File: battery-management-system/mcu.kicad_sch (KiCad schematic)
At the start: 28 parts, among them J11 I2C, J12 MCU_SUPPLY, J13 LEDS, U4 STM32L071CZTx, U5 ARM-JTAG-SWD, U8 AT24C512C, U9 NCT75DR2G

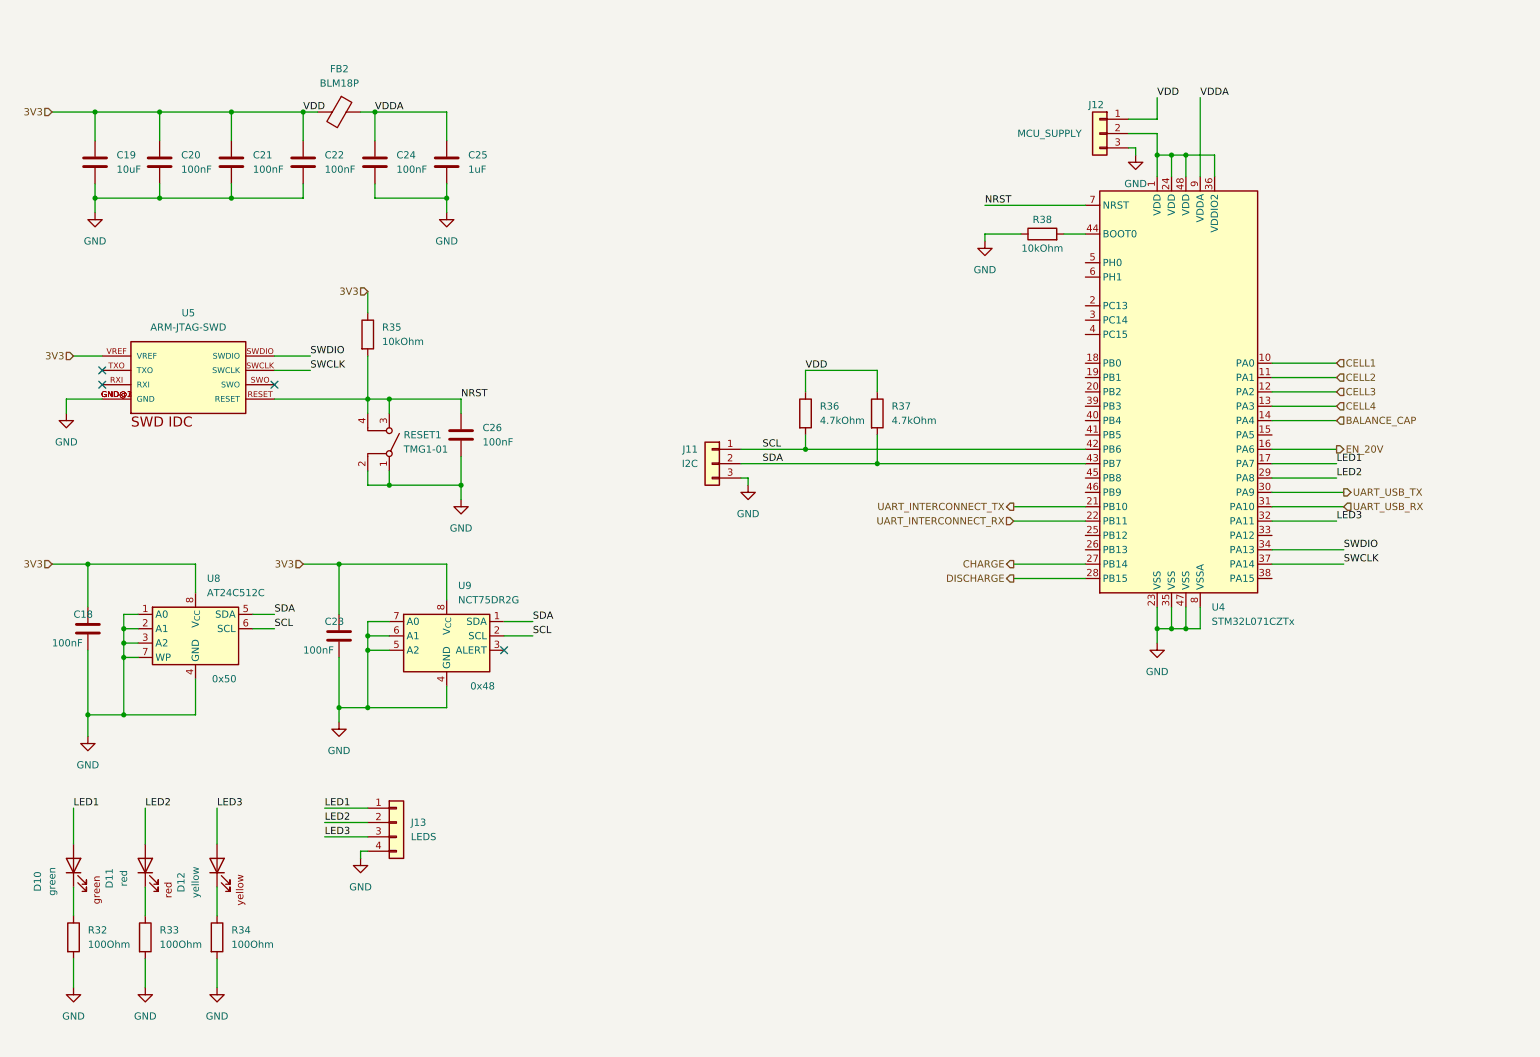
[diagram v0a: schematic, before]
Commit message: improve usage of net labels
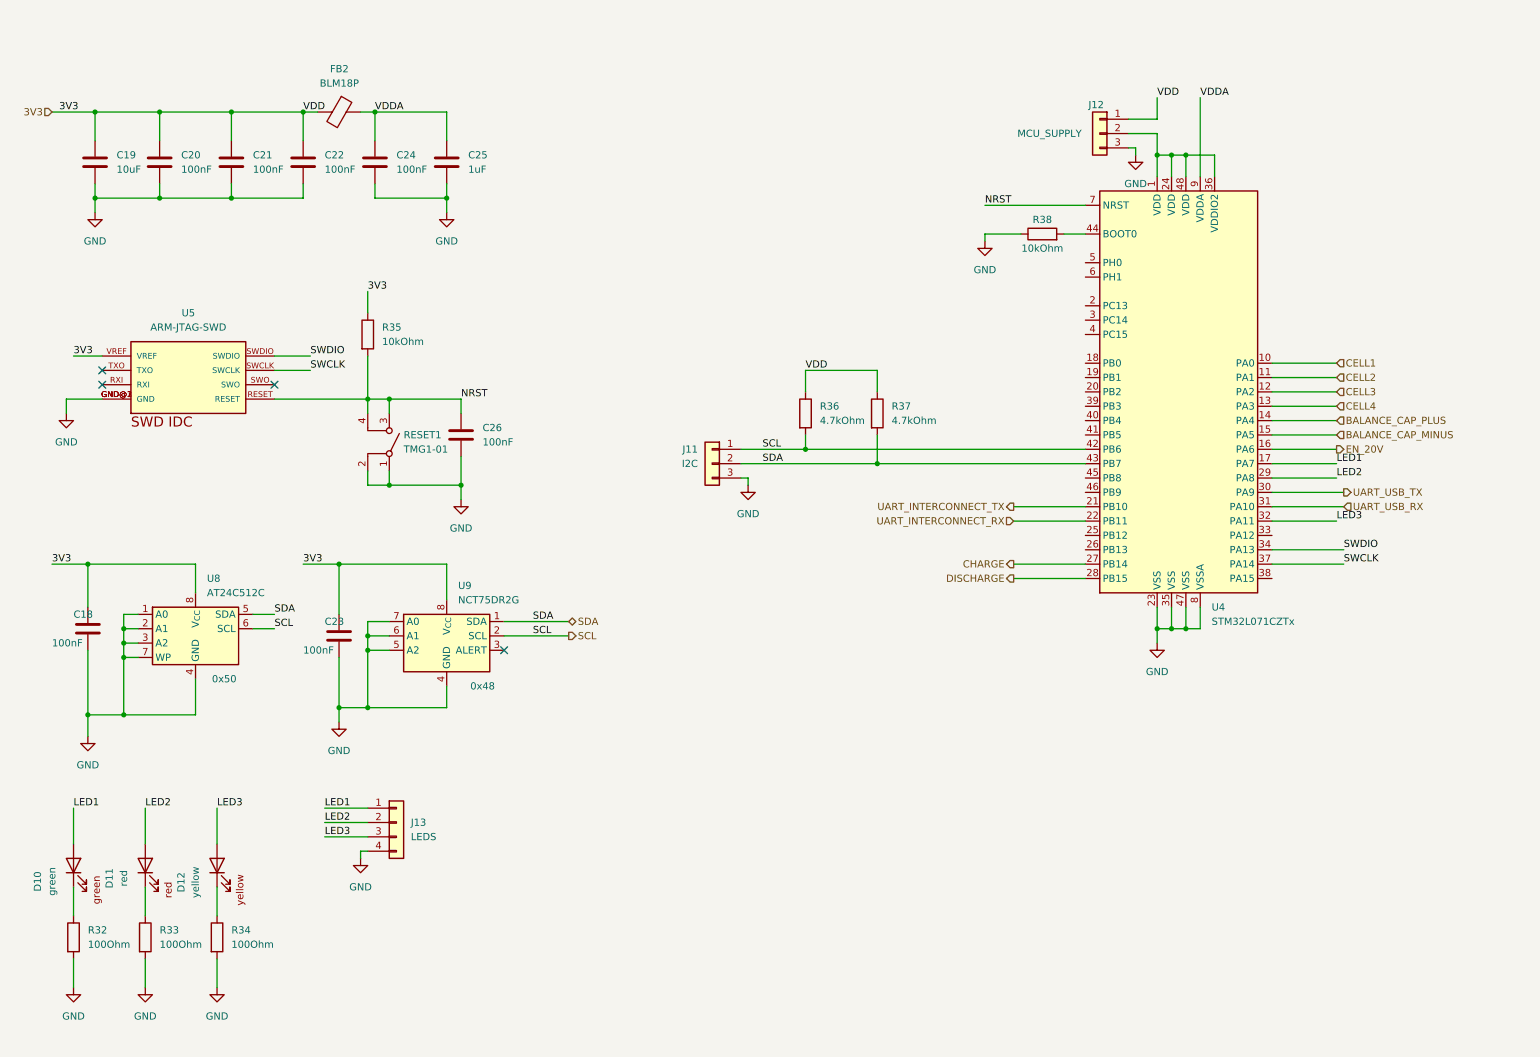
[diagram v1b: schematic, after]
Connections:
- net BALANCE_CAP_MINUS: now reaches U4.15 (PA5)
- net BALANCE_CAP renamed BALANCE_CAP_PLUS
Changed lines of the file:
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@@
     (stroke (width 0) (type default))
   )
-  (wire (pts (xy 104.14 120.65) (xy 109.22 120.65))
+  (wire (pts (xy 104.14 120.65) (xy 115.57 120.65))
     (stroke (width 0) (type default))
   )
@@
     (stroke (width 0) (type default))
   )
+  (wire (pts (xy 240.03 87.63) (xy 251.46 87.63))
+    (stroke (width 0) (type default))
+  )
   (wire (pts (xy 222.25 38.1) (xy 222.25 41.91))
     (stroke (width 0) (type default))
@@
     (stroke (width 0) (type default))
   )
-  (wire (pts (xy 104.14 123.19) (xy 109.22 123.19))
+  (wire (pts (xy 104.14 123.19) (xy 115.57 123.19))
     (stroke (width 0) (type default))
   )
@@
     (effects (font (size 1.27 1.27)) (justify left bottom))
   )
+  (label "3V3" (at 68.58 110.49 0) (fields_autoplaced)
+    (effects (font (size 1.27 1.27)) (justify left bottom))
+  )
   (label "SWCLK" (at 69.85 76.2 0) (fields_autoplaced)
     (effects (font (size 1.27 1.27)) (justify left bottom))
@@
     (effects (font (size 1.27 1.27)) (justify left bottom))
   )
+  (label "3V3" (at 80.01 62.23 0) (fields_autoplaced)
+    (effects (font (size 1.27 1.27)) (justify left bottom))
+  )
   (label "SDA" (at 109.22 120.65 0) (fields_autoplaced)
     (effects (font (size 1.27 1.27)) (justify left bottom))
   )
+  (label "3V3" (at 24.13 110.49 0) (fields_autoplaced)
+    (effects (font (size 1.27 1.27)) (justify left bottom))
+  )
   (label "SDA" (at 63.5 119.38 0) (fields_autoplaced)
     (effects (font (size 1.27 1.27)) (justify left bottom))
   )
+  (label "3V3" (at 25.4 30.48 0) (fields_autoplaced)
+    (effects (font (size 1.27 1.27)) (justify left bottom))
+  )
   (label "VDDA" (at 81.28 30.48 0) (fields_autoplaced)
     (effects (font (size 1.27 1.27)) (justify left bottom))
@@
     (effects (font (size 1.27 1.27)) (justify left bottom))
   )
+  (label "3V3" (at 27.94 73.66 0) (fields_autoplaced)
+    (effects (font (size 1.27 1.27)) (justify left bottom))
+  )
   (label "SCL" (at 63.5 121.92 0) (fields_autoplaced)
     (effects (font (size 1.27 1.27)) (justify left bottom))
@@
     (effects (font (size 1.27 1.27)) (justify left))
   )
-  (hierarchical_label "BALANCE_CAP" (shape input) (at 251.46 85.09 0) (fields_autoplaced)
+  (hierarchical_label "BALANCE_CAP_PLUS" (shape input) (at 251.46 85.09 0) (fields_autoplaced)
     (effects (font (size 1.27 1.27)) (justify left))
   )
   (hierarchical_label "EN_20V" (shape output) (at 251.46 90.17 0) (fields_autoplaced)
     (effects (font (size 1.27 1.27)) (justify left))
-  )
-  (hierarchical_label "3V3" (shape input) (at 80.01 62.23 180) (fields_autoplaced)
-    (effects (font (size 1.27 1.27)) (justify right))
   )
   (hierarchical_label "3V3" (shape input) (at 24.13 30.48 180) (fields_autoplaced)
@@
     (effects (font (size 1.27 1.27)) (justify left))
   )
-  (hierarchical_label "3V3" (shape input) (at 68.58 110.49 180) (fields_autoplaced)
-    (effects (font (size 1.27 1.27)) (justify right))
+  (hierarchical_label "SDA" (shape bidirectional) (at 115.57 120.65 0) (fields_autoplaced)
+    (effects (font (size 1.27 1.27)) (justify left))
+  )
+  (hierarchical_label "BALANCE_CAP_MINUS" (shape input) (at 251.46 87.63 0) (fields_autoplaced)
+    (effects (font (size 1.27 1.27)) (justify left))
+  )
+  (hierarchical_label "SCL" (shape output) (at 115.57 123.19 0) (fields_autoplaced)
+    (effects (font (size 1.27 1.27)) (justify left))
   )
   (hierarchical_label "UART_INTERCONNECT_RX" (shape input) (at 194.31 102.87 180) (fields_autoplaced)
     (effects (font (size 1.27 1.27)) (justify right))
   )
-  (hierarchical_label "3V3" (shape input) (at 27.94 73.66 180) (fields_autoplaced)
-    (effects (font (size 1.27 1.27)) (justify right))
-  )
   (hierarchical_label "CELL4" (shape input) (at 251.46 82.55 0) (fields_autoplaced)
     (effects (font (size 1.27 1.27)) (justify left))
@@
     (effects (font (size 1.27 1.27)) (justify left))
   )
-  (hierarchical_label "3V3" (shape input) (at 24.13 110.49 180) (fields_autoplaced)
-    (effects (font (size 1.27 1.27)) (justify right))
-  )
   (symbol (lib_id "benediktibk:C_1uF_SMD_0603_50V_10%") (at 93.98 39.37 0) (unit 1)

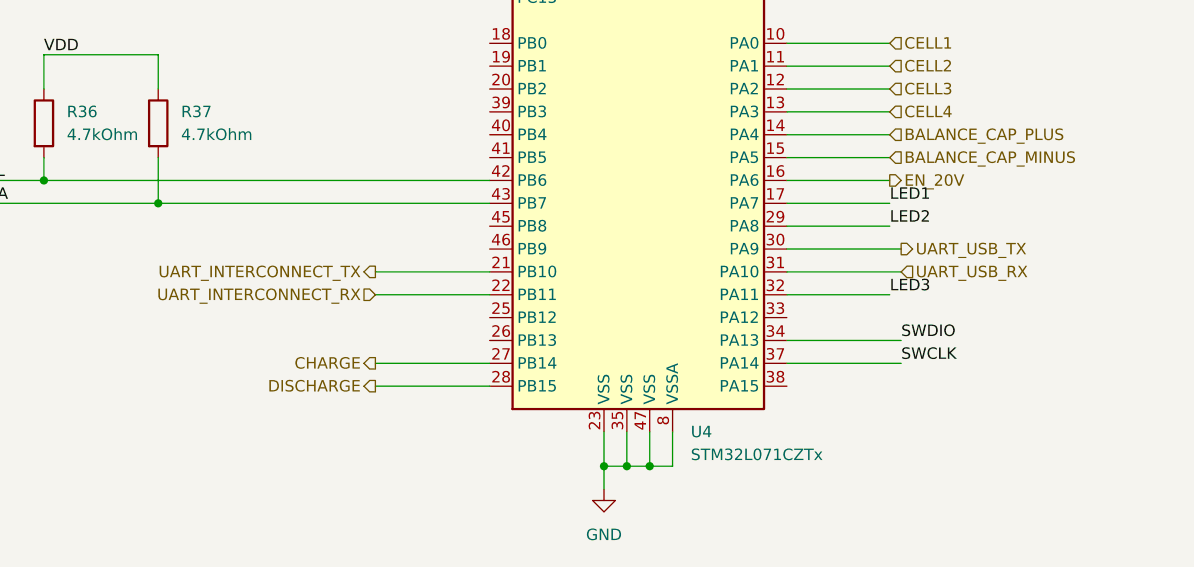
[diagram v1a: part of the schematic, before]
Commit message: add balancing sheet
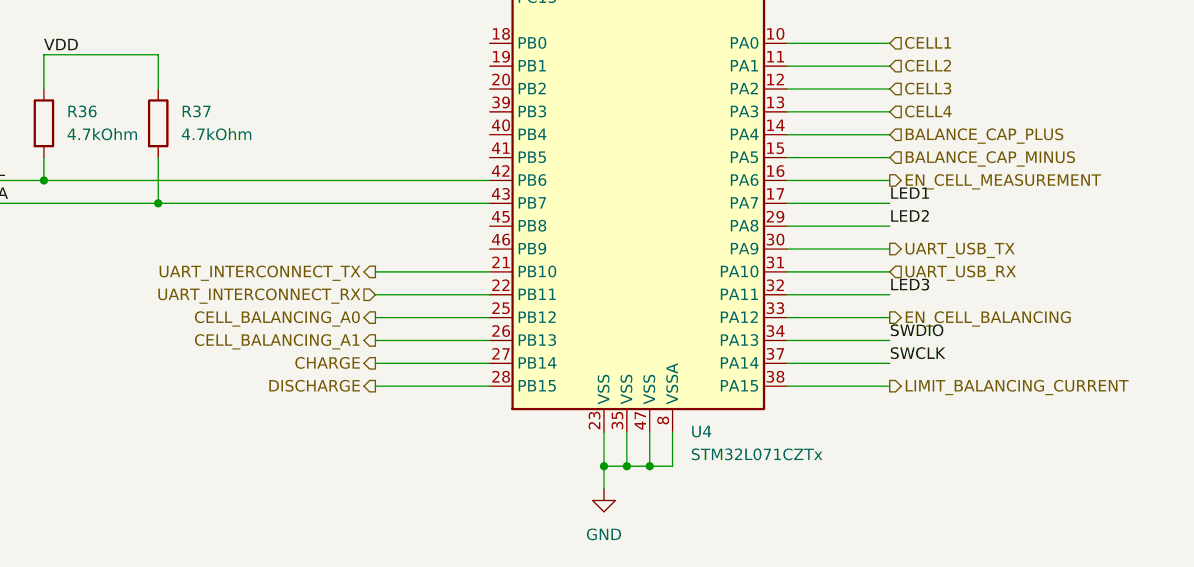
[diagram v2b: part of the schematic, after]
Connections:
- net CELL_BALANCING_A0: now reaches U4.25 (PB12)
- net CELL_BALANCING_A1: now reaches U4.26 (PB13)
- net EN_CELL_BALANCING: now reaches U4.33 (PA12)
- net LIMIT_BALANCING_CURRENT: now reaches U4.38 (PA15)
- net EN_20V renamed EN_CELL_MEASUREMENT
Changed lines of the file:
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@@
+    (stroke (width 0) (type default))
+  )
+  (wire (pts (xy 240.03 105.41) (xy 251.46 105.41))
     (stroke (width 0) (type default))
   )
@@
     (stroke (width 0) (type default))
   )
-  (wire (pts (xy 240.03 107.95) (xy 252.73 107.95))
+  (wire (pts (xy 240.03 107.95) (xy 251.46 107.95))
     (stroke (width 0) (type default))
   )
@@
     (stroke (width 0) (type default))
   )
-  (wire (pts (xy 240.03 110.49) (xy 252.73 110.49))
+  (wire (pts (xy 240.03 110.49) (xy 251.46 110.49))
     (stroke (width 0) (type default))
   )
@@
     (stroke (width 0) (type default))
   )
+  (wire (pts (xy 194.31 107.95) (xy 207.01 107.95))
+    (stroke (width 0) (type default))
+  )
   (wire (pts (xy 80.01 123.19) (xy 80.01 125.73))
     (stroke (width 0) (type default))
@@
     (stroke (width 0) (type default))
   )
+  (wire (pts (xy 194.31 105.41) (xy 207.01 105.41))
+    (stroke (width 0) (type default))
+  )
   (wire (pts (xy 80.01 125.73) (xy 83.82 125.73))
     (stroke (width 0) (type default))
@@
     (stroke (width 0) (type default))
   )
-  (wire (pts (xy 240.03 97.79) (xy 252.73 97.79))
+  (wire (pts (xy 240.03 97.79) (xy 251.46 97.79))
     (stroke (width 0) (type default))
   )
@@
     (stroke (width 0) (type default))
   )
-  (wire (pts (xy 240.03 100.33) (xy 252.73 100.33))
+  (wire (pts (xy 240.03 100.33) (xy 251.46 100.33))
     (stroke (width 0) (type default))
   )
@@
     (stroke (width 0) (type default))
   )
+  (wire (pts (xy 240.03 113.03) (xy 251.46 113.03))
+    (stroke (width 0) (type default))
+  )
   (wire (pts (xy 80.01 93.98) (xy 80.01 96.52))
     (stroke (width 0) (type default))
@@
     (effects (font (size 1.27 1.27)) (justify left bottom))
   )
-  (label "SWCLK" (at 252.73 110.49 0) (fields_autoplaced)
+  (label "SWCLK" (at 251.46 110.49 0) (fields_autoplaced)
     (effects (font (size 1.27 1.27)) (justify left bottom))
   )
@@
     (effects (font (size 1.27 1.27)) (justify left bottom))
   )
-  (label "SWDIO" (at 252.73 107.95 0) (fields_autoplaced)
+  (label "SWDIO" (at 251.46 107.95 0) (fields_autoplaced)
     (effects (font (size 1.27 1.27)) (justify left bottom))
   )
@@
     (effects (font (size 1.27 1.27)) (justify left bottom))
   )
-  (hierarchical_label "UART_USB_TX" (shape output) (at 252.73 97.79 0) (fields_autoplaced)
+  (hierarchical_label "UART_USB_TX" (shape output) (at 251.46 97.79 0) (fields_autoplaced)
     (effects (font (size 1.27 1.27)) (justify left))
   )
@@
     (effects (font (size 1.27 1.27)) (justify left))
   )
-  (hierarchical_label "EN_20V" (shape output) (at 251.46 90.17 0) (fields_autoplaced)
+  (hierarchical_label "EN_CELL_MEASUREMENT" (shape output) (at 251.46 90.17 0) (fields_autoplaced)
     (effects (font (size 1.27 1.27)) (justify left))
   )
@@
     (effects (font (size 1.27 1.27)) (justify right))
   )
-  (hierarchical_label "UART_USB_RX" (shape input) (at 252.73 100.33 0) (fields_autoplaced)
-    (effects (font (size 1.27 1.27)) (justify left))
+  (hierarchical_label "UART_USB_RX" (shape input) (at 251.46 100.33 0) (fields_autoplaced)
+    (effects (font (size 1.27 1.27)) (justify left))
+  )
+  (hierarchical_label "CELL_BALANCING_A0" (shape output) (at 194.31 105.41 180) (fields_autoplaced)
+    (effects (font (size 1.27 1.27)) (justify right))
   )
   (hierarchical_label "CELL1" (shape input) (at 251.46 74.93 0) (fields_autoplaced)
@@
     (effects (font (size 1.27 1.27)) (justify right))
   )
+  (hierarchical_label "LIMIT_BALANCING_CURRENT" (shape output) (at 251.46 113.03 0) (fields_autoplaced)
+    (effects (font (size 1.27 1.27)) (justify left))
+  )
   (hierarchical_label "CELL4" (shape input) (at 251.46 82.55 0) (fields_autoplaced)
     (effects (font (size 1.27 1.27)) (justify left))
@@
     (effects (font (size 1.27 1.27)) (justify left))
   )
+  (hierarchical_label "CELL_BALANCING_A1" (shape output) (at 194.31 107.95 180) (fields_autoplaced)
+    (effects (font (size 1.27 1.27)) (justify right))
+  )
+  (hierarchical_label "EN_CELL_BALANCING" (shape output) (at 251.46 105.41 0) (fields_autoplaced)
+    (effects (font (size 1.27 1.27)) (justify left))
+  )
